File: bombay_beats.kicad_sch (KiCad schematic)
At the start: 6 parts, among them SW1 SW_SPDT, U1 74HC165

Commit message: one sided version
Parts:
- added C1: 0.1u, Capacitor_SMD:C_0201_0603Metric, symbol Device:C
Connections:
- net GND: now also C1.2
- net VCC: now also C1.1

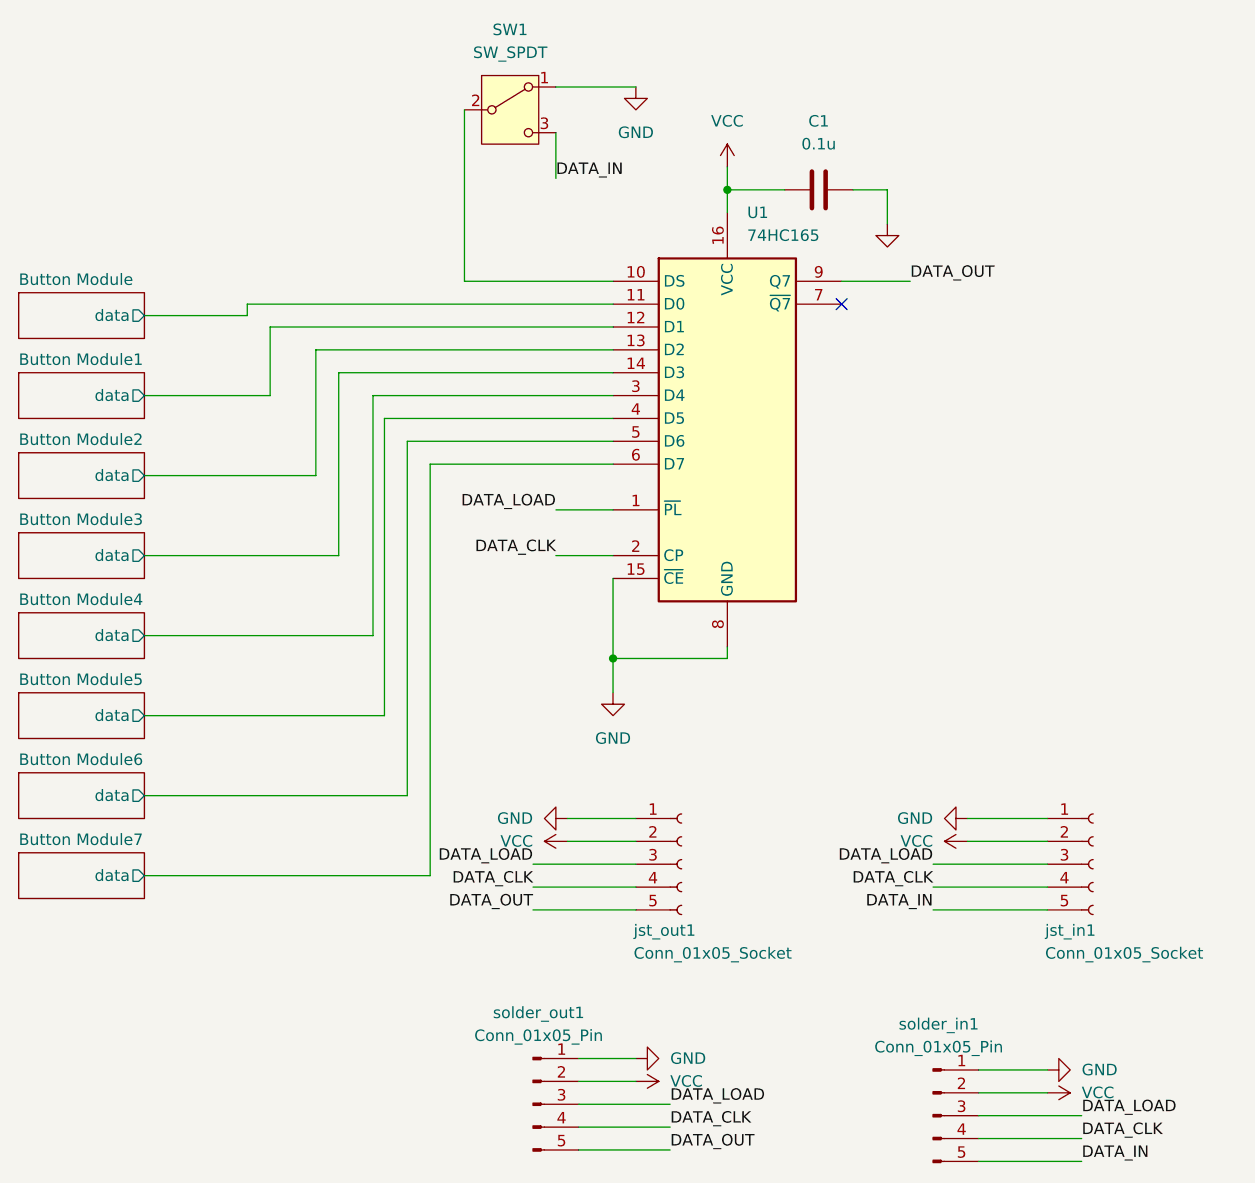
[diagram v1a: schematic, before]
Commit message: finalize one sided smd version
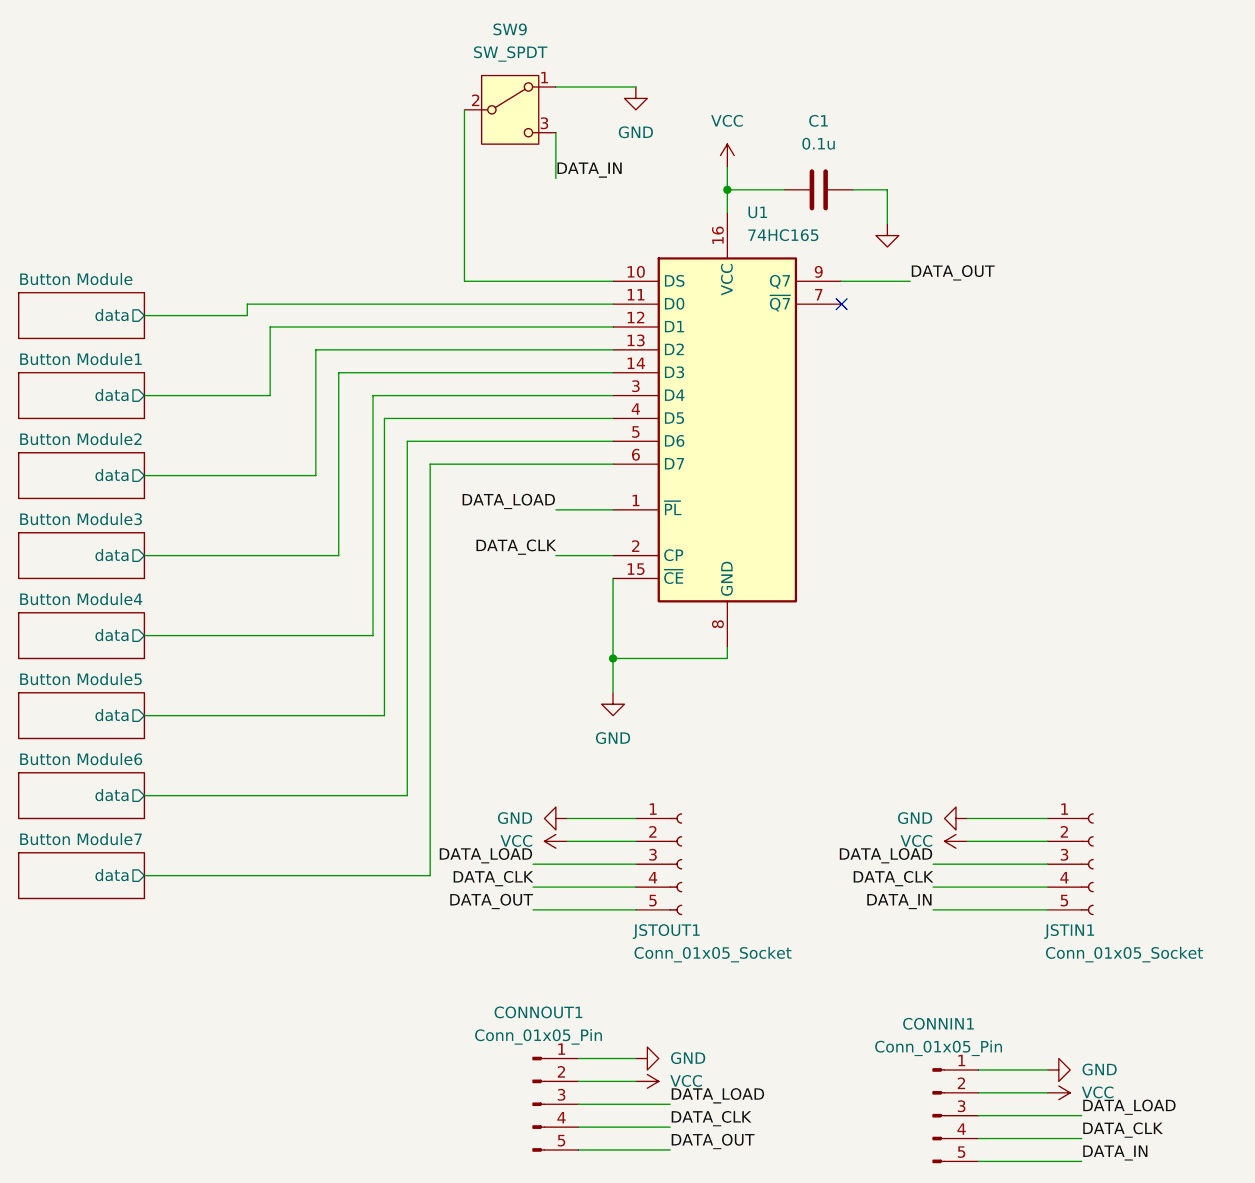
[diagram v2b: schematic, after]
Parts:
- C1: LCSC Part #  (none) -> C1322361; Part number C1322361 -> (none)
- JSTIN1: renamed from jst_in1; LCSC Part #  (none) -> C136657; Part number C136657 -> (none)
- JSTOUT1: renamed from jst_out1; LCSC Part #  (none) -> C136657; Part number C136657 -> (none)
- U1: LCSC Part #  (none) -> C80093; Part number C80093 -> (none)
- renumbered solder_in1 to CONNIN1, solder_out1 to CONNOUT1, SW1 to SW9
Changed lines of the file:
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@@
 		(dnp no)
 		(fields_autoplaced yes)
-		(property "Reference" "solder_in1"
+		(property "Reference" "CONNIN1"
 			(at 151.765 124.46 0)
 			(effects
@@
 			)
 		)
-		(property "part_number" ""
+		(property "LCSC Part # " ""
 			(at 151.13 134.62 0)
 			(effects
@@
 			(project "bombay_beats"
 				(path "/4c45dfb4-652a-4480-93b8-479ee7e6e64f"
-					(reference "solder_in1")
+					(reference "CONNIN1")
 					(unit 1)
 				)
@@
 		(on_board yes)
 		(dnp no)
-		(property "Reference" "jst_in1"
+		(property "Reference" "JSTIN1"
 			(at 163.576 114.046 0)
 			(effects
@@
 			)
 		)
-		(property "Part number" "C136657"
+		(property "LCSC Part # " "C136657"
 			(at 168.91 106.68 0)
 			(effects
@@
 			)
 		)
-		(property "part_number" ""
-			(at 168.91 106.68 0)
-			(effects
-				(font
-					(size 1.27 1.27)
-				)
-				(hide yes)
-			)
-		)
 		(pin "2"
 		)
@@
 			(project "bombay_beats"
 				(path "/4c45dfb4-652a-4480-93b8-479ee7e6e64f"
-					(reference "jst_in1")
+					(reference "JSTIN1")
 					(unit 1)
 				)
@@
 		(dnp no)
 		(fields_autoplaced yes)
-		(property "Reference" "solder_out1"
+		(property "Reference" "CONNOUT1"
 			(at 107.315 123.19 0)
 			(effects
@@
 			)
 		)
-		(property "part_number" ""
+		(property "LCSC Part # " ""
 			(at 106.68 133.35 0)
 			(effects
@@
 			(project "bombay_beats"
 				(path "/4c45dfb4-652a-4480-93b8-479ee7e6e64f"
-					(reference "solder_out1")
+					(reference "CONNOUT1")
 					(unit 1)
 				)
@@
 			)
 		)
-		(property "Part number" "C80093"
-			(at 128.27 57.15 0)
-			(effects
-				(font
-					(size 1.27 1.27)
-				)
-				(hide yes)
-			)
-		)
-		(property "part_number" ""
+		(property "LCSC Part # " "C80093"
 			(at 128.27 57.15 0)
 			(effects
@@
 		(dnp no)
 		(fields_autoplaced yes)
-		(property "Reference" "SW1"
+		(property "Reference" "SW9"
 			(at 104.14 13.97 0)
 			(effects
@@
 			)
 		)
-		(property "part_number" ""
+		(property "LCSC Part # " ""
 			(at 104.14 22.86 0)
 			(effects
@@
 			(project "bombay_beats"
 				(path "/4c45dfb4-652a-4480-93b8-479ee7e6e64f"
-					(reference "SW1")
+					(reference "SW9")
 					(unit 1)
 				)
@@
 		(on_board yes)
 		(dnp no)
-		(property "Reference" "jst_out1"
+		(property "Reference" "JSTOUT1"
 			(at 117.856 114.046 0)
 			(effects
@@
 			)
 		)
-		(property "Part number" "C136657"
+		(property "LCSC Part # " "C136657"
 			(at 123.19 106.68 0)
 			(effects
@@
 			)
 		)
-		(property "part_number" ""
-			(at 123.19 106.68 0)
-			(effects
-				(font
-					(size 1.27 1.27)
-				)
-				(hide yes)
-			)
-		)
 		(pin "2"
 		)
@@
 			(project "bombay_beats"
 				(path "/4c45dfb4-652a-4480-93b8-479ee7e6e64f"
-					(reference "jst_out1")
+					(reference "JSTOUT1")
 					(unit 1)
 				)
@@
 			)
 		)
-		(property "Part number" "C1322361"
+		(property "LCSC Part # " "C1322361"
 			(at 138.43 31.75 0)
 			(effects
@@
 			(at 138.43 31.75 0)
 			(effects
-				(font
-					(size 1.27 1.27)
-				)
-				(hide yes)
-			)
-		)
-		(property "part_number" ""
-			(at 138.43 31.75 0)
-			(effects

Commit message: replace footprints for through hole version
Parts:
- C1: footprint Capacitor_SMD:C_0201_0603Metric -> Capacitor_THT:CP_Axial_L10.0mm_D4.5mm_P15.00mm_Horizontal
- JSTIN1, JSTOUT1: footprint Connector_JST:JST_SH_SM05B-SRSS-TB_1x05-1MP_P1.00mm_Horizontal -> Connector_JST:JST_VH_B5P-VH-FB-B_1x05_P3.96mm_Vertical
- SW9: footprint Button_Switch_SMD:SW_SPDT_PCM12 -> Button_Switch_THT:SW_Slide-03_Wuerth-WS-SLTV_10x2.5x6.4_P2.54mm
- U1: footprint Package_SO:TSSOP-16-1EP_4.4x5mm_P0.65mm_EP3x3mm_ThermalVias -> Package_DIP:DIP-16_W10.16mm
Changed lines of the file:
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@@
 			)
 		)
-		(property "Footprint" "Connector_JST:JST_SH_SM05B-SRSS-TB_1x05-1MP_P1.00mm_Horizontal"
+		(property "Footprint" "Connector_JST:JST_VH_B5P-VH-FB-B_1x05_P3.96mm_Vertical"
 			(at 168.91 106.68 0)
 			(effects
@@
 			)
 		)
-		(property "Footprint" "Package_SO:TSSOP-16-1EP_4.4x5mm_P0.65mm_EP3x3mm_ThermalVias"
+		(property "Footprint" "Package_DIP:DIP-16_W10.16mm"
 			(at 128.27 57.15 0)
 			(effects
@@
 			)
 		)
-		(property "Footprint" "Button_Switch_SMD:SW_SPDT_PCM12"
+		(property "Footprint" "Button_Switch_THT:SW_Slide-03_Wuerth-WS-SLTV_10x2.5x6.4_P2.54mm"
 			(at 104.14 22.86 0)
 			(effects
@@
 			)
 		)
-		(property "Footprint" "Connector_JST:JST_SH_SM05B-SRSS-TB_1x05-1MP_P1.00mm_Horizontal"
+		(property "Footprint" "Connector_JST:JST_VH_B5P-VH-FB-B_1x05_P3.96mm_Vertical"
 			(at 123.19 106.68 0)
 			(effects
@@
 			)
 		)
-		(property "Footprint" "Capacitor_SMD:C_0201_0603Metric"
+		(property "Footprint" "Capacitor_THT:CP_Axial_L10.0mm_D4.5mm_P15.00mm_Horizontal"
 			(at 142.24 30.7848 0)
 			(effects

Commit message: production files
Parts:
- JSTIN1, JSTOUT1: footprint Connector_JST:JST_VH_B5P-VH-FB-B_1x05_P3.96mm_Vertical -> Connector_PinHeader_1.00mm:PinHeader_1x05_P1.00mm_Vertical
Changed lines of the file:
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@@
 			)
 		)
-		(property "Footprint" "Connector_JST:JST_VH_B5P-VH-FB-B_1x05_P3.96mm_Vertical"
+		(property "Footprint" "Connector_PinHeader_1.00mm:PinHeader_1x05_P1.00mm_Vertical"
 			(at 168.91 106.68 0)
 			(effects
@@
 			)
 		)
-		(property "Footprint" "Connector_JST:JST_VH_B5P-VH-FB-B_1x05_P3.96mm_Vertical"
+		(property "Footprint" "Connector_PinHeader_1.00mm:PinHeader_1x05_P1.00mm_Vertical"
 			(at 123.19 106.68 0)
 			(effects
